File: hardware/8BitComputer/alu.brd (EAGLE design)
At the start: 100 x 75 mm, 32 parts, among them IC1 SN74LS245NE4, IC2 SN74LS86AN, IC3 SN74LS283N, IC4 SN74LS86AN, IC8 SN74LS283N

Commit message: alu routed
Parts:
- added LED9: RED, leds:LED3MM-NS
- added R9: 100 R, passives:0805
- moved U$1 27.0 mm to (69.8, 48.3)
- moved IC4 21.3 mm to (10.2, 67.3), turned to 180 degrees
- moved C3 16.6 mm to (81.3, 45.7), turned to 180 degrees
- moved IC2 16.6 mm to (83.8, 64.8), turned to 180 degrees
- moved C2 13.3 mm to (12.7, 3.81), turned to 0 degrees
- moved IC3 13.3 mm to (10.2, 25.4), turned to 180 degrees
- moved IC8 12.0 mm to (83.8, 26.7), turned to 180 degrees
- moved C5 11.6 mm to (87.5, 5.08), turned to 0 degrees
- moved C1 10.1 mm to (14.0, 47.8), turned to 0 degrees
- moved J5 6.48 mm to (11.4, 31.8)
- moved IC1 5.08 mm to (50.0, 37.5)
- moved J2 4.20 mm to (43.3, 6.73)
- moved LED1 3.81 mm to (68.6, 24.1)
- moved LED2 3.81 mm to (63.5, 24.1)
- moved LED3 3.81 mm to (58.4, 24.1)
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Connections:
- removed net N$6: J5.5
- new net N$10: IC3.9, R9.1
- new net N$11: LED9.A, R9.2
- net ALUOUT_OE: now also J5.3; no longer J5.2
- net AO_DIR: now also J5.2; no longer J5.3
- net AR2O_2: now also IC8.15
- net AR2O_3: no longer IC8.15
- net CARRY_ADD: now also IC3.7, IC8.9; no longer IC3.9, IC8.7
- net GND: now also J5.5, LED9.K
- net OP_SUBTRACT: now also IC8.7; no longer IC8.9
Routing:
- net VCC5V: track 0.00 -> 249.2 mm
- net GND: track 0.00 -> 224.0 mm
- net OP_SUBTRACT: track 0.00 -> 172.5 mm
- net AO_1: track 0.00 -> 78.5 mm
- net CARRY_ADD: track 0.00 -> 69.0 mm
- net AR2_0: track 0.00 -> 66.4 mm
- net AO_0: track 0.00 -> 65.6 mm
- net AR2O_6: track 0.00 -> 64.7 mm
- net AO_5: track 0.00 -> 59.9 mm
- net AR2_1: track 0.00 -> 58.5 mm
- net AR2O_5: track 0.00 -> 57.2 mm
- net AR2O_2: track 0.00 -> 56.7 mm
- net AR1_BUS0: track 0.00 -> 55.8 mm
- net AO_6: track 0.00 -> 53.6 mm
- net AR2O_1: track 0.00 -> 53.6 mm
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- added copper zone on layer 16, net GND
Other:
- board text added: "74LS283N"
- board text added: "74LS86"
- board text added: "ALU"
- board text added: "ALU TO BUS"
- board text added: "REG 1 IN"
- board text added: "REG 2 IN"

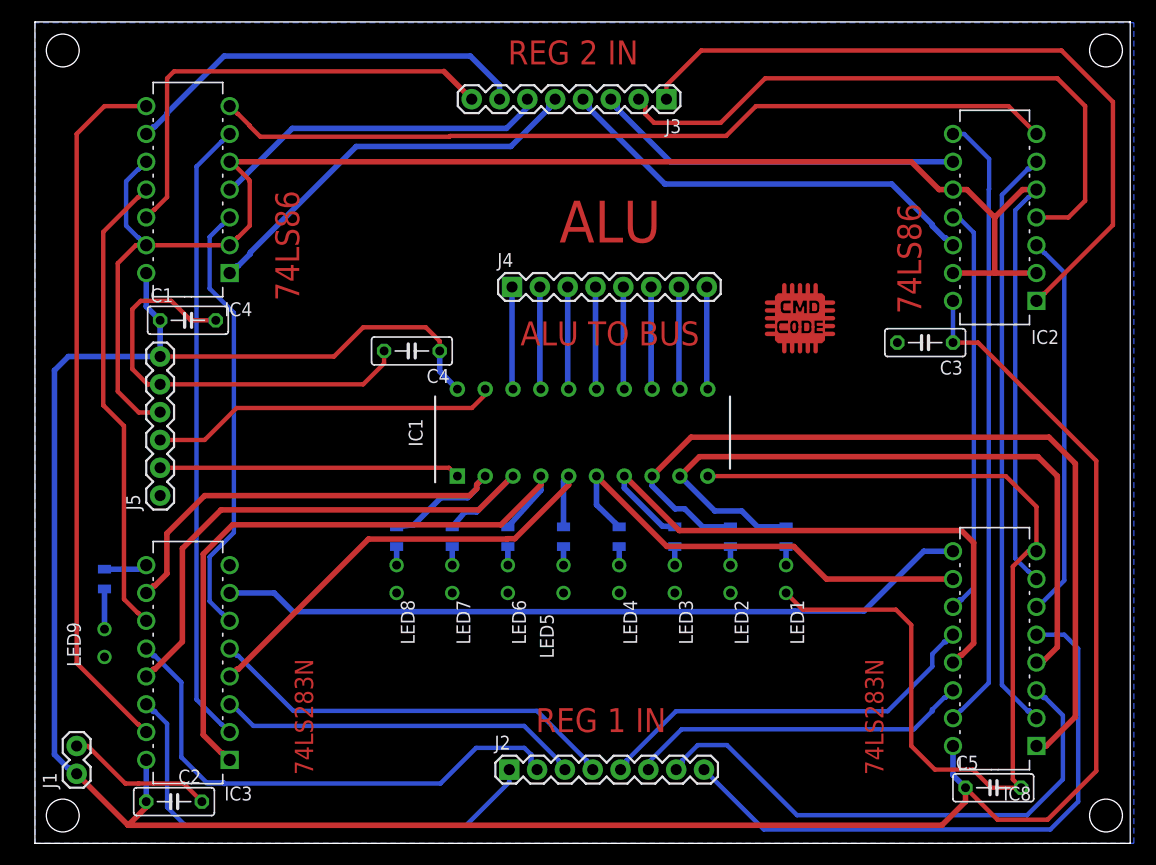
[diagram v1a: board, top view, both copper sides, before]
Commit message: adding static ram chip updated all other boards to remove led resistors that aren't needed
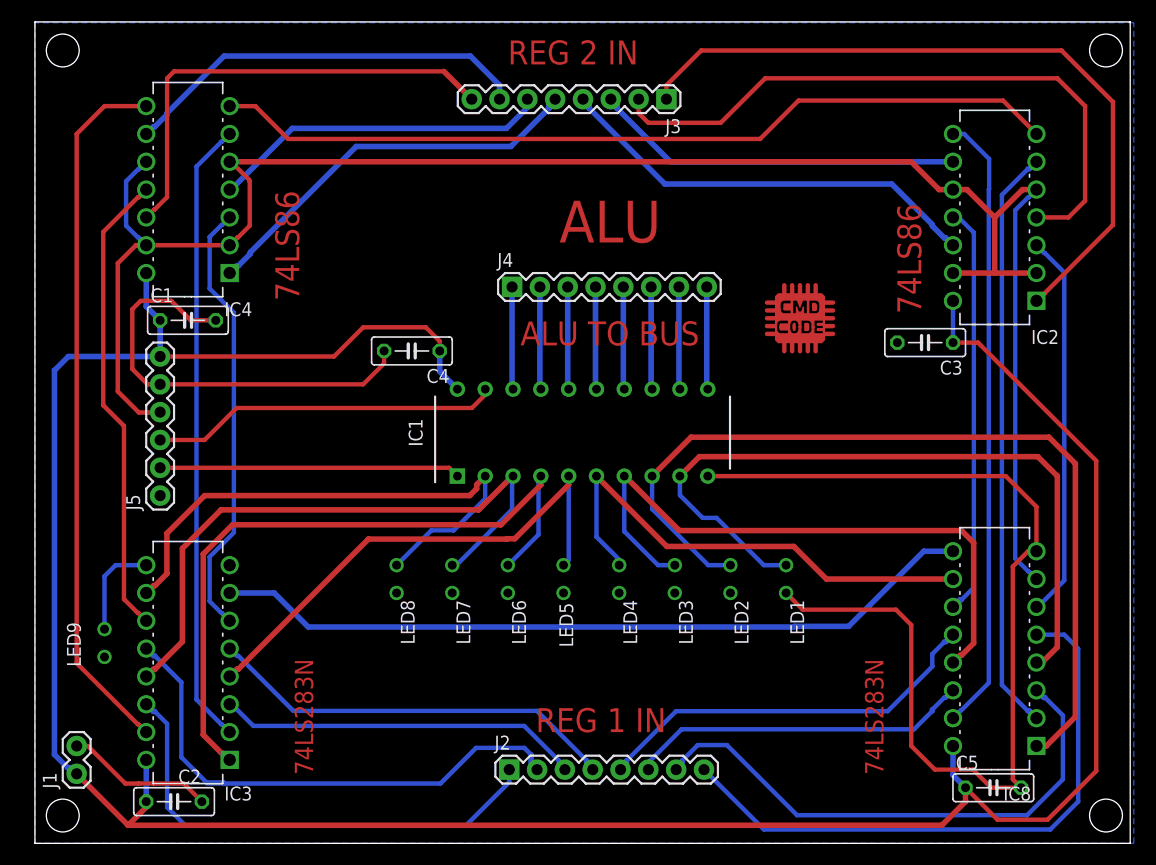
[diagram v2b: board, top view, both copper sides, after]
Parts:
- removed R1, R2, R3, R4, R5, R6, R7, R8, R9: 100 R, passives:0805
- LED1, LED2, LED3, LED4, LED5, LED6, LED7, LED8: value (none) -> YELLOW
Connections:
- removed net N$1: LED1.A, R8.1
- removed net N$11: LED9.A, R9.2
- removed net N$2: LED2.A, R7.1
- removed net N$3: LED3.A, R6.1
- removed net N$4: LED4.A, R5.1
- removed net N$5: LED5.A, R4.1
- removed net N$7: LED6.A, R3.1
- removed net N$8: LED7.A, R2.1
- removed net N$9: LED8.A, R1.1
- net AO_0: now also LED1.A; no longer R8.2
- net AO_1: now also LED2.A; no longer R7.2
- net AO_2: now also LED3.A; no longer R6.2
- net AO_3: now also LED4.A; no longer R5.2
- net AO_4: now also LED5.A; no longer R4.2
- net AO_5: now also LED6.A; no longer R3.2
- net AO_6: now also LED7.A; no longer R2.2
- net AO_7: now also LED8.A; no longer R1.2
- net N$10: now also LED9.A; no longer R9.1
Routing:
- net N$10: track 3.96 -> 9.06 mm
- net AO_2: track 53.4 -> 57.1 mm
- net N$11: track 3.67 -> 0.00 mm
- net AO_5: track 59.9 -> 63.5 mm
- net AO_4: track 43.8 -> 47.3 mm
- net AO_3: track 41.9 -> 45.4 mm
- net AO_6: track 53.6 -> 56.7 mm
- net AO_1: track 78.5 -> 81.2 mm
- net AO_7: track 47.9 -> 50.4 mm
- net AO_0: track 65.6 -> 68.1 mm
- net N$9: track 1.70 -> 0.00 mm
- net N$8: track 1.70 -> 0.00 mm
- net N$7: track 1.70 -> 0.00 mm
- net N$5: track 1.70 -> 0.00 mm
- net N$4: track 1.70 -> 0.00 mm
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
